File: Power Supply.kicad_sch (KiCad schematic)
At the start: 6 parts, among them U2 TPS61023DRLT

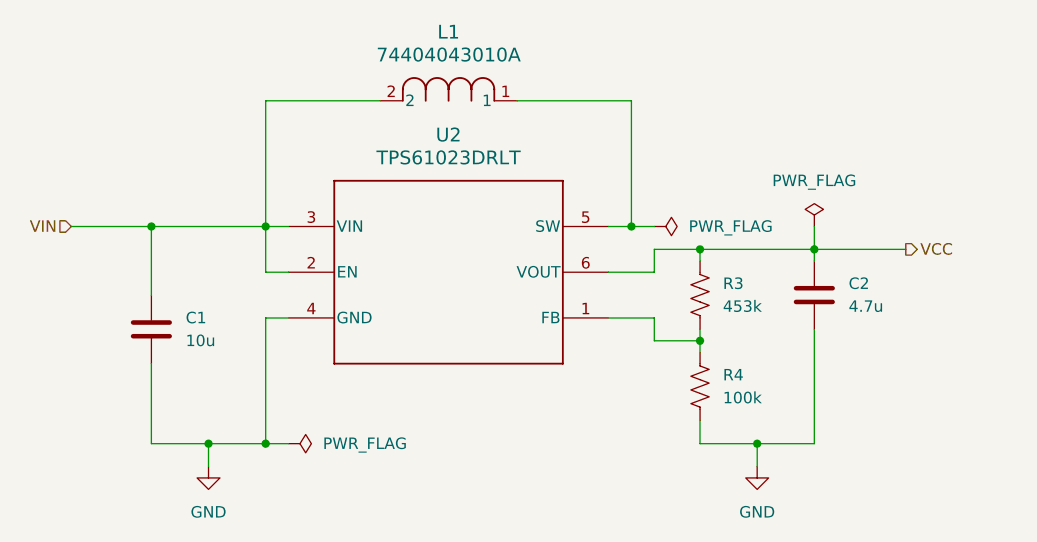
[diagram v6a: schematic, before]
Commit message: switched to full-sized ESP32 S3 WROOM and redid PCB layout
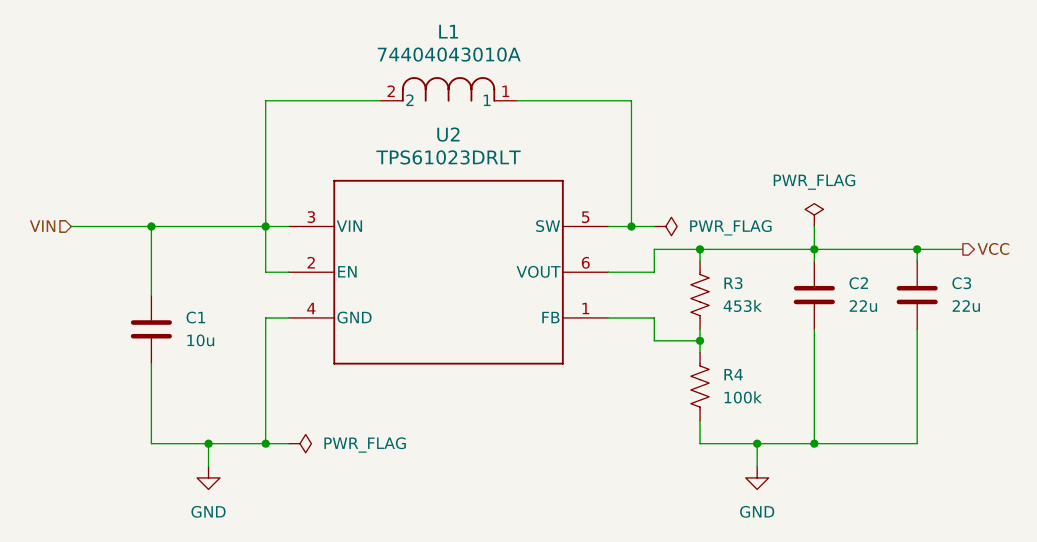
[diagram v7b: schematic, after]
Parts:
- added C3: 22u, Capacitor_SMD:C_0603_1608Metric, symbol Device:C
- C1: footprint Capacitor_SMD:C_0402_1005Metric -> Capacitor_SMD:C_0603_1608Metric
- C2: value 4.7u -> 22u; footprint Capacitor_SMD:C_0402_1005Metric -> Capacitor_SMD:C_0603_1608Metric
- R3, R4: footprint Resistor_SMD:R_0402_1005Metric -> Capacitor_SMD:C_0603_1608Metric
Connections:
- net GND: now also C3.2
- net VCC: now also C3.1
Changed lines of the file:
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@@
   (junction (at 118.11 121.92) (diameter 0) (color 0 0 0 0)
   )
+  (junction (at 185.42 121.92) (diameter 0) (color 0 0 0 0)
+  )
   (junction (at 172.72 100.33) (diameter 0) (color 0 0 0 0)
   )
   (junction (at 172.72 110.49) (diameter 0) (color 0 0 0 0)
   )
+  (junction (at 196.85 100.33) (diameter 0) (color 0 0 0 0)
+  )
   (junction (at 165.1 97.79) (diameter 0) (color 0 0 0 0)
   )
@@
     (stroke (width 0) (type default))
   )
+  (wire (pts (xy 196.85 109.22) (xy 196.85 121.92))
+    (stroke (width 0) (type default))
+  )
   (wire (pts (xy 124.46 121.92) (xy 127 121.92))
     (stroke (width 0) (type default))
@@
     (stroke (width 0) (type default))
   )
-  (wire (pts (xy 185.42 100.33) (xy 195.58 100.33))
+  (wire (pts (xy 185.42 100.33) (xy 196.85 100.33))
     (stroke (width 0) (type default))
   )
@@
     (stroke (width 0) (type default))
   )
+  (wire (pts (xy 196.85 121.92) (xy 185.42 121.92))
+    (stroke (width 0) (type default))
+  )
   (wire (pts (xy 124.46 107.95) (xy 124.46 121.92))
     (stroke (width 0) (type default))
@@
   )
   (wire (pts (xy 165.1 97.79) (xy 167.64 97.79))
+    (stroke (width 0) (type default))
+  )
+  (wire (pts (xy 196.85 100.33) (xy 201.93 100.33))
+    (stroke (width 0) (type default))
+  )
+  (wire (pts (xy 196.85 100.33) (xy 196.85 101.6))
     (stroke (width 0) (type default))
   )
@@
     (effects (font (size 1.27 1.27)) (justify right))
   )
-  (hierarchical_label "VCC" (shape output) (at 195.58 100.33 0) (fields_autoplaced)
+  (hierarchical_label "VCC" (shape output) (at 201.93 100.33 0) (fields_autoplaced)
     (effects (font (size 1.27 1.27)) (justify left))
   )
@@
       (effects (font (size 1.27 1.27)) (justify left))
     )
-    (property "Footprint" "Resistor_SMD:R_0402_1005Metric" (at 173.736 115.824 90)
+    (property "Footprint" "Capacitor_SMD:C_0603_1608Metric" (at 173.736 115.824 90)
       (effects (font (size 1.27 1.27)) hide)
     )
@@
       (effects (font (size 1.27 1.27)) (justify left))
     )
-    (property "Footprint" "Capacitor_SMD:C_0402_1005Metric" (at 112.7252 113.03 0)
+    (property "Footprint" "Capacitor_SMD:C_0603_1608Metric" (at 112.7252 113.03 0)
       (effects (font (size 1.27 1.27)) hide)
     )
@@
         (path "/b002c3bf-fc58-4993-80f7-7914d3aa1ac9/97ab50b4-0765-4242-8cdd-feb1ed8d7056"
           (reference "C1") (unit 1)
+        )
+      )
+    )
+  )
+  (symbol (lib_id "Device:C") (at 196.85 105.41 0) (unit 1)
+    (in_bom yes) (on_board yes) (dnp no) (fields_autoplaced)
+    (property "Reference" "C3" (at 200.66 104.14 0)
+      (effects (font (size 1.27 1.27)) (justify left))
+    )
+    (property "Value" "22u" (at 200.66 106.68 0)
+      (effects (font (size 1.27 1.27)) (justify left))
+    )
+    (property "Footprint" "Capacitor_SMD:C_0603_1608Metric" (at 197.8152 109.22 0)
+      (effects (font (size 1.27 1.27)) hide)
+    )
+    (property "Datasheet" "~" (at 196.85 105.41 0)
+      (effects (font (size 1.27 1.27)) hide)
+    )
+    (property "MPN " "C2686246" (at 196.85 105.41 0)
+      (effects (font (size 1.27 1.27)) hide)
+    )
+    (pin "1")
+    (pin "2")
+    (instances
+      (project "key-fob-pcb"
+        (path "/b002c3bf-fc58-4993-80f7-7914d3aa1ac9/97ab50b4-0765-4242-8cdd-feb1ed8d7056"
+          (reference "C3") (unit 1)
         )
       )
@@
       (effects (font (size 1.27 1.27)) (justify left))
     )
-    (property "Footprint" "Resistor_SMD:R_0402_1005Metric" (at 173.736 105.664 90)
+    (property "Footprint" "Capacitor_SMD:C_0603_1608Metric" (at 173.736 105.664 90)
       (effects (font (size 1.27 1.27)) hide)
     )
@@
       (effects (font (size 1.27 1.27)) (justify left))
     )
-    (property "Value" "4.7u" (at 189.23 106.68 0)
-      (effects (font (size 1.27 1.27)) (justify left))
-    )
-    (property "Footprint" "Capacitor_SMD:C_0402_1005Metric" (at 186.3852 109.22 0)
-      (effects (font (size 1.27 1.27)) hide)
-    )
+    (property "Value" "22u" (at 189.23 106.68 0)
+      (effects (font (size 1.27 1.27)) (justify left))
+    )
+    (property "Footprint" "Capacitor_SMD:C_0603_1608Metric" (at 186.3852 109.22 0)
+      (effects (font (size 1.27 1.27)) hide)
+    )
